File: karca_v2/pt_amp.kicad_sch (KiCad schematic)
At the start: 18 parts, among them J6 Screw_Terminal_01x10, U10 TLV9304xD, U11 MCP3208, U12 NUP4202, U8 TPS7A24, U9 TLV9304xD

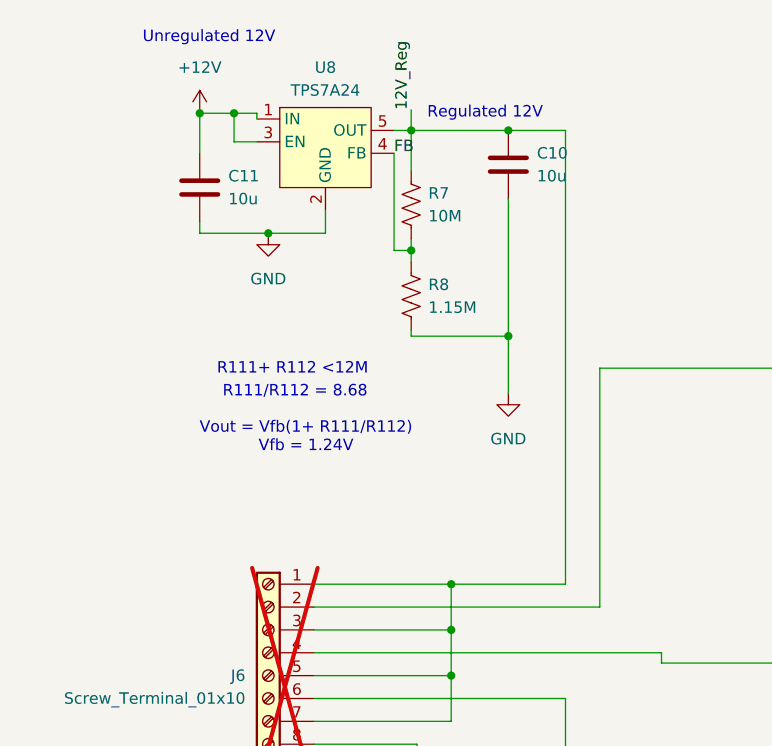
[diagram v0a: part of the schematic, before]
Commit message: Swapped IRF3708 FETs for AO3400 for more compact package
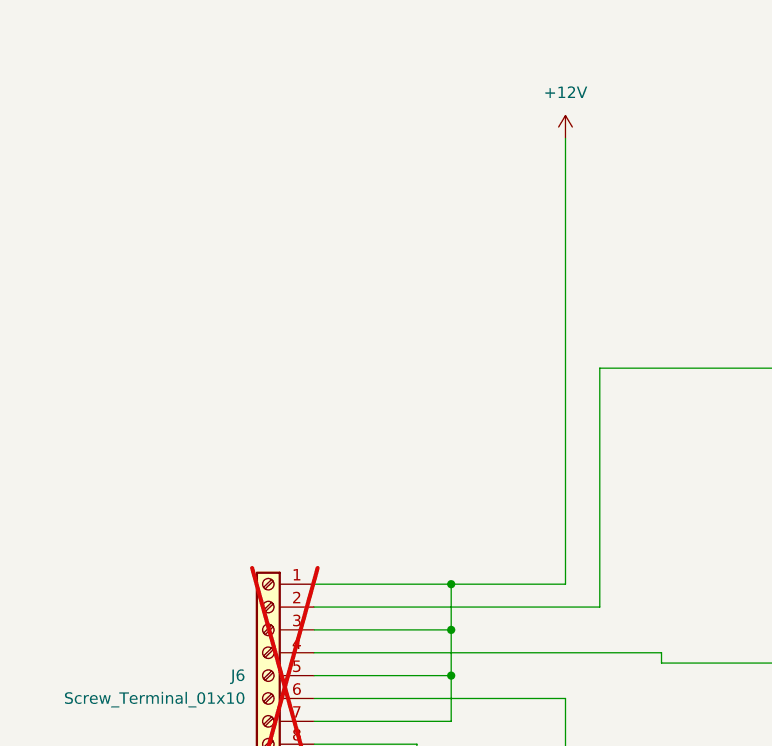
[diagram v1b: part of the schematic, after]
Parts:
- removed C10, C11: 10u, Capacitor_SMD:C_1206_3216Metric, symbol Device:C
- removed R7: 10M, Resistor_SMD:R_1206_3216Metric, symbol Device:R_US
- removed R8: 1.15M, Resistor_SMD:R_1206_3216Metric, symbol Device:R_US
- removed U8: TPS7A24, Package_TO_SOT_SMD:SOT-23-5, symbol karca_lib:TPS7A24
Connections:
- net 12V_Reg is gone; now on net +12V: J6.1 (Pin_1), J6.3 (Pin_3), J6.5 (Pin_5), J6.7 (Pin_7)
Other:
- note removed: "R111+ R112 <12M"
- note removed: "R111/R112 = 8.68"
- note removed: "Regulated 12V"
- note removed: "Unregulated 12V"
- note removed: "Vout = Vfb(1+ R111/R112) Vfb = 1.24V"

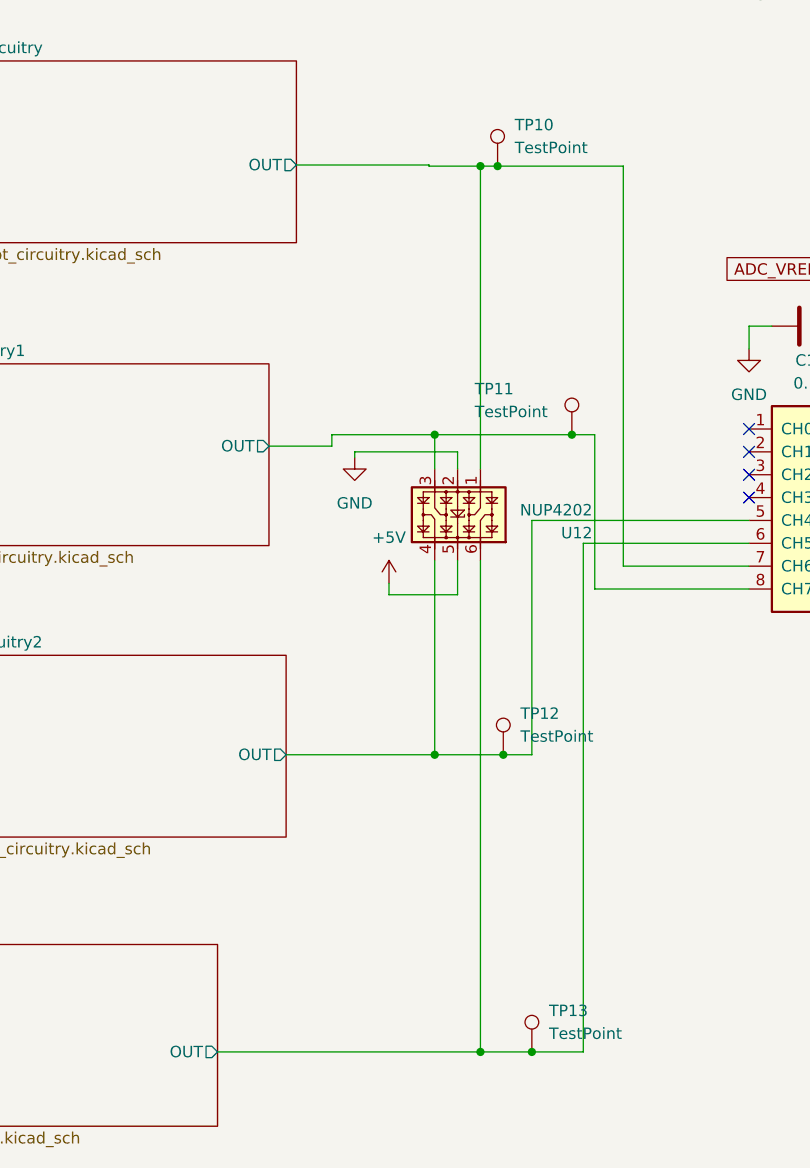
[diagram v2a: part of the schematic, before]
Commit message: fixed all routing. Now need to clean up vias
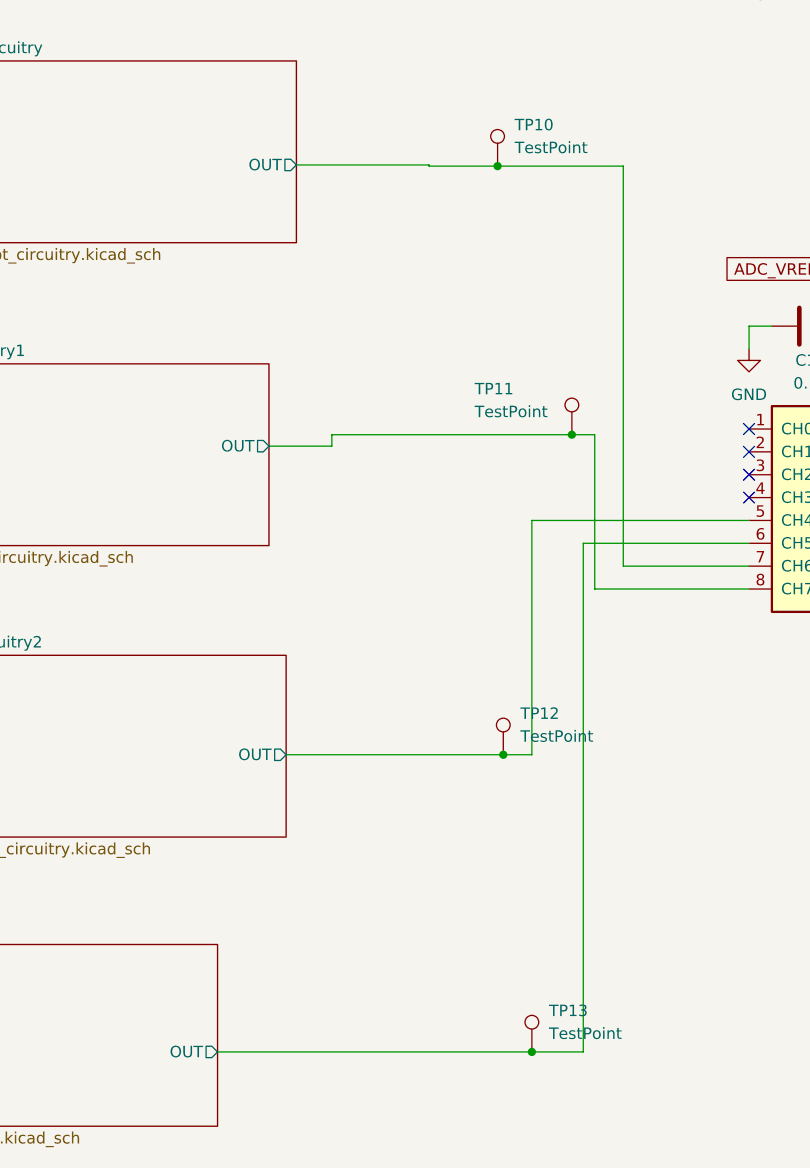
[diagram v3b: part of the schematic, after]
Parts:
- removed U12: NUP4202, Package_TO_SOT_SMD:SOT-363_SC-70-6, symbol Power_Protection:NUP4202
